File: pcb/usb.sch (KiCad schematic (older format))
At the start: 0 parts

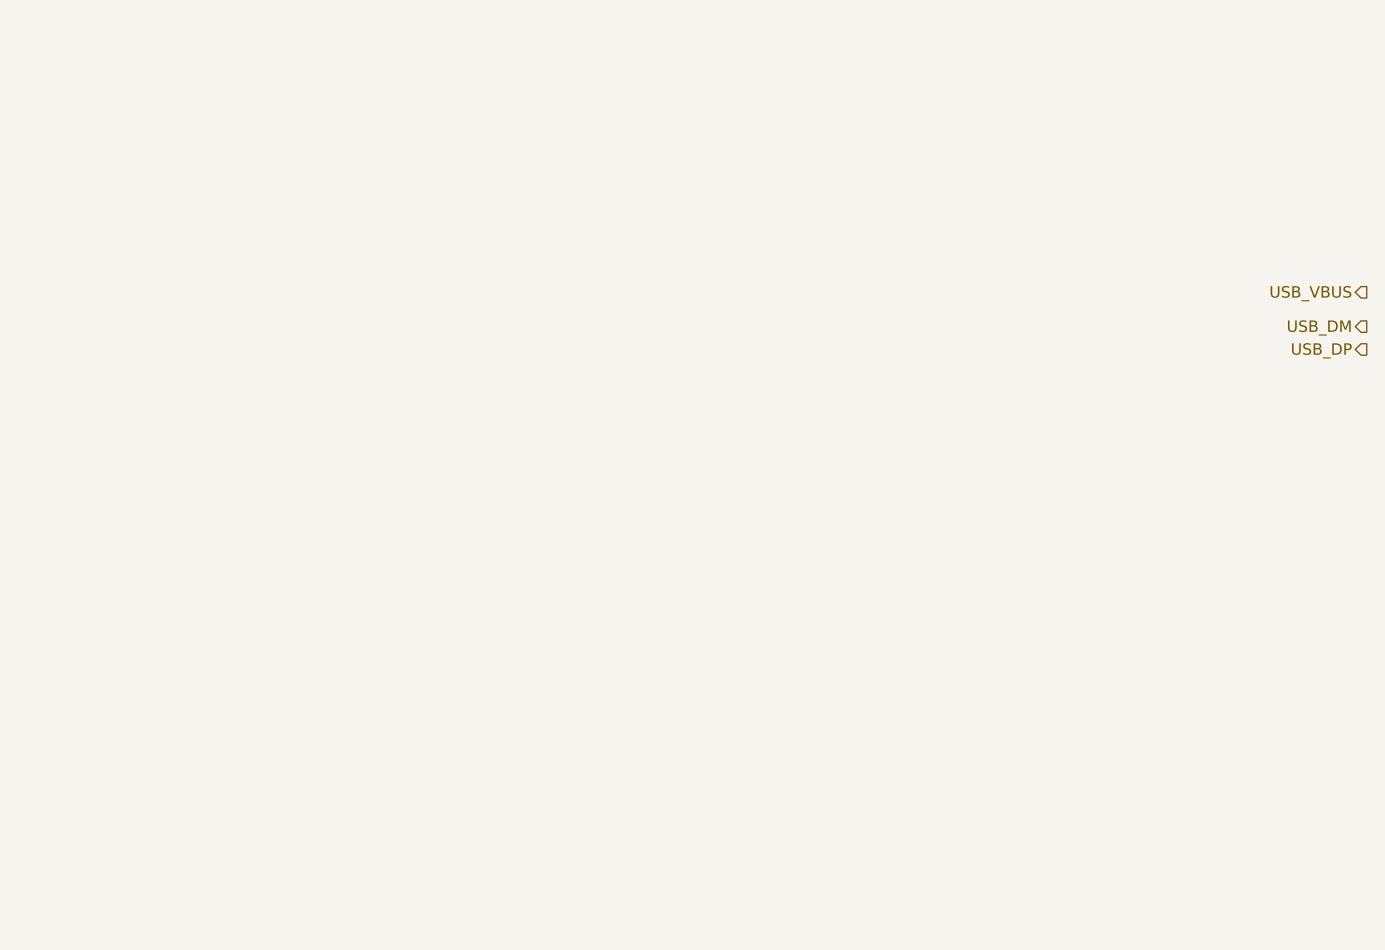
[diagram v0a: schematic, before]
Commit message: SCH: missing signal logic and level shifting
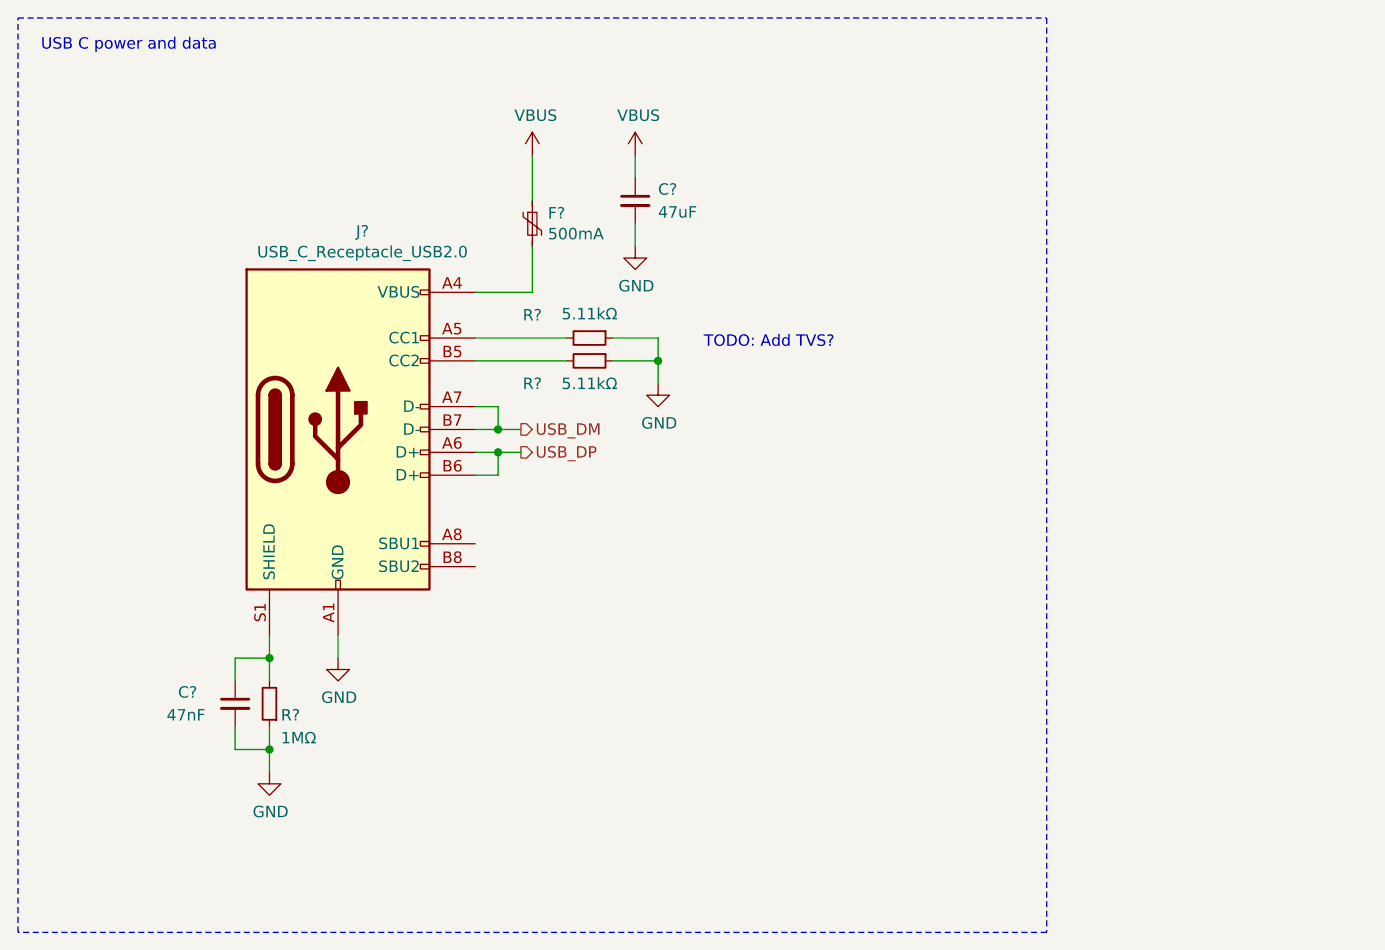
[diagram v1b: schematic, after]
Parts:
- added C?: 47nF, symbol Device:C_Small
- added C?: 47uF, symbol Device:C_Small
- added F?: 500mA, symbol Device:Polyfuse_Small
- added J?: USB_C_Receptacle_USB2.0, symbol Connector:USB_C_Receptacle_USB2.0
- added R? (x2): 5.11kΩ, symbol Device:R_Small
- added R?: 1MΩ, symbol Device:R_Small
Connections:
- net USB_DM: now also J?.A7 (D-), J?.B7 (D-)
- net USB_DP: now also J?.A6 (D+), J?.B6 (D+)
- new net: F?.2, J?.A4 (VBUS), J?.A9 (VBUS), J?.B4 (VBUS), J?.B9 (VBUS)
- new net: J?.A5 (CC1), R?.2
- new net: J?.B5 (CC2), R?.2
- new net: C?.1, J?.S1 (SHIELD), R?.2
- new net GND: C?.2, C?.2, J?.A1 (GND), J?.A12 (GND), J?.B1 (GND), J?.B12 (GND), R?.1, R?.1, R?.1
- new net VBUS: C?.1, F?.1
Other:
- note added: "TODO: Add TVS?\n"
- note added: "USB C power and data"
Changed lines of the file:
@@
 $Descr A4 11693 8268
 encoding utf-8
-Sheet 2 8
-Title ""
-Date ""
-Rev ""
-Comp ""
-Comment1 ""
+Sheet 6 7
+Title "Modular-programmer"
+Date "2020-03-03"
+Rev "1.0"
+Comp "Pepetech"
+Comment1 "Creative Commons Attribution-ShareAlike 4.0 International License"
 Comment2 ""
-Comment3 ""
-Comment4 ""
+Comment3 "Co-designer: João Silva"
+Comment4 "Designer: Rafael Silva"
 $EndDescr
-Text HLabel 9400 2850 0    50   Output ~ 0
+Text HLabel 5700 3300 2    50   Output ~ 0
 USB_DM
-Text HLabel 9400 2950 0    50   Output ~ 0
+Text HLabel 5700 3400 2    50   Output ~ 0
 USB_DP
-Text HLabel 9400 2700 0    50   Output ~ 0
-USB_VBUS
+$Comp
+L Connector:USB_C_Receptacle_USB2.0 J?
+U 1 1 5E6B6DFC
+P 4900 3300
+F 0 "J?" H 5007 4167 50  0000 C CNN
+F 1 "USB_C_Receptacle_USB2.0" H 5007 4076 50  0000 C CNN
+F 2 "" H 5050 3300 50  0001 C CNN
+F 3 "https://www.usb.org/sites/default/files/documents/usb_type-c.zip" H 5050 3300 50  0001 C CNN
+	1    4900 3300
+	1    0    0    -1
+$EndComp
+Wire Wire Line
+	5500 3400 5600 3400
+Wire Wire Line
+	5500 3500 5600 3500
+Wire Wire Line
+	5600 3500 5600 3400
+Connection ~ 5600 3400
+Wire Wire Line
+	5600 3400 5700 3400
+Wire Wire Line
+	5500 3200 5600 3200
+Wire Wire Line
+	5600 3200 5600 3300
+Wire Wire Line
+	5600 3300 5700 3300
+Wire Wire Line
+	5500 3300 5600 3300
+Connection ~ 5600 3300
+Wire Wire Line
+	5750 2700 5750 2500
+$Comp
+L Device:Polyfuse_Small F?
+U 1 1 5E6B9537
+P 5750 2400
+F 0 "F?" H 5818 2446 50  0000 L CNN
+F 1 "500mA" H 5818 2355 50  0000 L CNN
+F 2 "" H 5800 2200 50  0001 L CNN
+F 3 "~" H 5750 2400 50  0001 C CNN
+	1    5750 2400
+	1    0    0    -1
+$EndComp
+Wire Wire Line
+	5750 2300 5750 2100
+$Comp
+L Device:R_Small R?
+U 1 1 5E6BB888
+P 6000 2900
+F 0 "R?" V 5900 2650 50  0000 C CNN
+F 1 "5.11kΩ" V 5895 2900 50  0000 C CNN
+F 2 "" H 6000 2900 50  0001 C CNN
+F 3 "~" H 6000 2900 50  0001 C CNN
+	1    6000 2900
+	0    1    1    0
+$EndComp
+$Comp
+L Device:R_Small R?
+U 1 1 5E6BC592
+P 6000 3000
+F 0 "R?" V 6100 2750 50  0000 C CNN
+F 1 "5.11kΩ" V 6100 3000 50  0000 C CNN
+F 2 "" H 6000 3000 50  0001 C CNN
+F 3 "~" H 6000 3000 50  0001 C CNN
+	1    6000 3000
+	0    1    1    0
+$EndComp
+Wire Wire Line
+	6100 2900 6300 2900
+Wire Wire Line
+	6300 2900 6300 3000
+Wire Wire Line
+	6100 3000 6300 3000
+Connection ~ 6300 3000
+Wire Wire Line
+	6300 3000 6300 3100
+$Comp
+L power:GND #PWR?
+U 1 1 5E6BE57B
+P 6300 3100
+F 0 "#PWR?" H 6300 2850 50  0001 C CNN
+F 1 "GND" H 6305 2927 50  0000 C CNN
+F 2 "" H 6300 3100 50  0001 C CNN
+F 3 "" H 6300 3100 50  0001 C CNN
+	1    6300 3100
+	1    0    0    -1
+$EndComp
+Wire Wire Line
+	4900 4200 4900 4300
+Wire Wire Line
+	4600 4200 4600 4300
+Wire Wire Line
+	4600 4300 4450 4300
+Wire Wire Line
+	4450 4300 4450 4400
+Connection ~ 4600 4300
+Wire Wire Line
+	4600 4300 4600 4400
+$Comp
+L Device:R_Small R?
+U 1 1 5E6BF283
+P 4600 4500
+F 0 "R?" H 4550 4550 50  0000 R CNN
+F 1 "1MΩ" H 4550 4650 50  0000 R CNN
+F 2 "" H 4600 4500 50  0001 C CNN
+F 3 "~" H 4600 4500 50  0001 C CNN
+	1    4600 4500
+	-1   0    0    1
+$EndComp
+$Comp
+L Device:C_Small C?
+U 1 1 5E6BFCD2
+P 4450 4500
+F 0 "C?" H 4200 4550 50  0000 L CNN
+F 1 "47nF" H 4150 4450 50  0000 L CNN
+F 2 "" H 4450 4500 50  0001 C CNN
+F 3 "~" H 4450 4500 50  0001 C CNN
+	1    4450 4500
+	1    0    0    -1
+$EndComp
+Wire Wire Line
+	4450 4600 4450 4700
+Wire Wire Line
+	4450 4700 4600 4700
+Wire Wire Line
+	4600 4700 4600 4800
+Wire Wire Line
+	4600 4600 4600 4700
+Connection ~ 4600 4700
+$Comp
+L power:GND #PWR?
+U 1 1 5E6C0B4E
+P 4600 4800
+F 0 "#PWR?" H 4600 4550 50  0001 C CNN
+F 1 "GND" H 4605 4627 50  0000 C CNN
+F 2 "" H 4600 4800 50  0001 C CNN
+F 3 "" H 4600 4800 50  0001 C CNN
+	1    4600 4800
+	1    0    0    -1
+$EndComp
+$Comp
+L power:GND #PWR?
+U 1 1 5E6C1141
+P 4900 4300
+F 0 "#PWR?" H 4900 4050 50  0001 C CNN
+F 1 "GND" H 4905 4127 50  0000 C CNN
+F 2 "" H 4900 4300 50  0001 C CNN
+F 3 "" H 4900 4300 50  0001 C CNN
+	1    4900 4300
+	1    0    0    -1
+$EndComp
+$Comp
+L power:VBUS #PWR?
+U 1 1 5E8C6541
+P 5750 2100
+F 0 "#PWR?" H 5750 1950 50  0001 C CNN
+F 1 "VBUS" H 5765 2273 50  0000 C CNN
+F 2 "" H 5750 2100 50  0001 C CNN
+F 3 "" H 5750 2100 50  0001 C CNN
+	1    5750 2100
+	1    0    0    -1
+$EndComp
+Wire Notes Line
+	3500 1500 8000 1500
+Wire Notes Line
+	8000 1500 8000 5500
+Wire Notes Line
+	8000 5500 3500 5500
+Wire Notes Line
+	3500 5500 3500 1500
+Text Notes 3600 1650 0    50   ~ 0
+USB C power and data
+$Comp
+L power:VBUS #PWR?
+U 1 1 5E950B45
+P 6200 2100
+F 0 "#PWR?" H 6200 1950 50  0001 C CNN
+F 1 "VBUS" H 6215 2273 50  0000 C CNN
+F 2 "" H 6200 2100 50  0001 C CNN
+F 3 "" H 6200 2100 50  0001 C CNN
+	1    6200 2100
+	1    0    0    -1
+$EndComp
+Wire Wire Line
+	6200 2100 6200 2200
+$Comp
+L Device:C_Small C?
+U 1 1 5E9512A0
+P 6200 2300
+F 0 "C?" H 6300 2350 50  0000 L CNN
+F 1 "47uF" H 6300 2250 50  0000 L CNN
+F 2 "" H 6200 2300 50  0001 C CNN
+F 3 "~" H 6200 2300 50  0001 C CNN
+	1    6200 2300
+	1    0    0    -1
+$EndComp
+Wire Wire Line
+	6200 2400 6200 2500
+$Comp
+L power:GND #PWR?
+U 1 1 5E952003
+P 6200 2500
+F 0 "#PWR?" H 6200 2250 50  0001 C CNN
+F 1 "GND" H 6205 2327 50  0000 C CNN
+F 2 "" H 6200 2500 50  0001 C CNN
+F 3 "" H 6200 2500 50  0001 C CNN
+	1    6200 2500
+	1    0    0    -1
+$EndComp
+Text Notes 6500 2950 0    50   ~ 0
+TODO: Add TVS?\n
+Wire Wire Line
+	5750 2700 5500 2700
+Wire Wire Line
+	5500 2900 5900 2900
+Wire Wire Line
+	5500 3000 5900 3000
 $EndSCHEMATC

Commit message: SCH: minor changes
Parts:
- removed F?: 500mA, symbol Device:Polyfuse_Small
- added TH?: Thermistor_PTC, symbol Device:Thermistor_PTC
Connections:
- net VBUS: now also TH?.1
- net at J?.A4 (VBUS), J?.A9 (VBUS), J?.B4 (VBUS)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: now also TH?.2
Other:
- moved on the sheet: C?
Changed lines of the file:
@@
 	5500 3300 5600 3300
 Connection ~ 5600 3300
-Wire Wire Line
-	5750 2700 5750 2500
-$Comp
-L Device:Polyfuse_Small F?
-U 1 1 5E6B9537
-P 5750 2400
-F 0 "F?" H 5818 2446 50  0000 L CNN
-F 1 "500mA" H 5818 2355 50  0000 L CNN
-F 2 "" H 5800 2200 50  0001 L CNN
-F 3 "~" H 5750 2400 50  0001 C CNN
-	1    5750 2400
-	1    0    0    -1
-$EndComp
-Wire Wire Line
-	5750 2300 5750 2100
 $Comp
 L Device:R_Small R?
@@
 L power:VBUS #PWR?
 U 1 1 5E950B45
-P 6200 2100
-F 0 "#PWR?" H 6200 1950 50  0001 C CNN
-F 1 "VBUS" H 6215 2273 50  0000 C CNN
-F 2 "" H 6200 2100 50  0001 C CNN
-F 3 "" H 6200 2100 50  0001 C CNN
-	1    6200 2100
+P 6700 2200
+F 0 "#PWR?" H 6700 2050 50  0001 C CNN
+F 1 "VBUS" H 6715 2373 50  0000 C CNN
+F 2 "" H 6700 2200 50  0001 C CNN
+F 3 "" H 6700 2200 50  0001 C CNN
+	1    6700 2200
 	1    0    0    -1
 $EndComp
 Wire Wire Line
-	6200 2100 6200 2200
+	6700 2200 6700 2300
 $Comp
 L Device:C_Small C?
 U 1 1 5E9512A0
-P 6200 2300
-F 0 "C?" H 6300 2350 50  0000 L CNN
-F 1 "47uF" H 6300 2250 50  0000 L CNN
-F 2 "" H 6200 2300 50  0001 C CNN
-F 3 "~" H 6200 2300 50  0001 C CNN
-	1    6200 2300
+P 6700 2400
+F 0 "C?" H 6800 2450 50  0000 L CNN
+F 1 "47uF" H 6800 2350 50  0000 L CNN
+F 2 "" H 6700 2400 50  0001 C CNN
+F 3 "~" H 6700 2400 50  0001 C CNN
+	1    6700 2400
 	1    0    0    -1
 $EndComp
 Wire Wire Line
-	6200 2400 6200 2500
+	6700 2500 6700 2600
 $Comp
 L power:GND #PWR?
 U 1 1 5E952003
-P 6200 2500
-F 0 "#PWR?" H 6200 2250 50  0001 C CNN
-F 1 "GND" H 6205 2327 50  0000 C CNN
-F 2 "" H 6200 2500 50  0001 C CNN
-F 3 "" H 6200 2500 50  0001 C CNN
-	1    6200 2500
+P 6700 2600
+F 0 "#PWR?" H 6700 2350 50  0001 C CNN
+F 1 "GND" H 6705 2427 50  0000 C CNN
+F 2 "" H 6700 2600 50  0001 C CNN
+F 3 "" H 6700 2600 50  0001 C CNN
+	1    6700 2600
 	1    0    0    -1
 $EndComp
@@
 Wire Wire Line
 	5500 3000 5900 3000
+$Comp
+L Device:Thermistor_PTC TH?
+U 1 1 5EB8559A
+P 5750 2400
+F 0 "TH?" H 5848 2446 50  0000 L CNN
+F 1 "Thermistor_PTC" H 5848 2355 50  0000 L CNN
+F 2 "" H 5800 2200 50  0001 L CNN
+F 3 "~" H 5750 2400 50  0001 C CNN
+	1    5750 2400
+	1    0    0    -1
+$EndComp
+Wire Wire Line
+	5750 2250 5750 2100
+Wire Wire Line
+	5750 2700 5750 2550
 $EndSCHEMATC

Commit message: SCH: slight changes
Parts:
- removed C?: 47uF, symbol Device:C_Small
- added C602: 10nF, Capacitor_SMD:C_0603_1608Metric_Pad1.05x0.95mm_HandSolder, symbol Device:C_Small
- added D601, D602: PGB1010603, Diode_SMD:D_0603_1608Metric_Pad1.05x0.95mm_HandSolder, symbol Device:D_TVS_ALT
- added FB601: 600R/0.5A, Inductor_SMD:L_0603_1608Metric_Pad1.05x0.95mm_HandSolder, symbol Device:Ferrite_Bead_Small
- C601: renamed from C?; footprint (none) -> Capacitor_SMD:C_0603_1608Metric_Pad1.05x0.95mm_HandSolder
- J601: renamed from J?; footprint (none) -> Connector_USB:USB_C_Receptacle_HRO_TYPE-C-31-M-12
- R601: renamed from R?; footprint (none) -> Resistor_SMD:R_0603_1608Metric_Pad1.05x0.95mm_HandSolder
- R602, R603: renamed from R?; value 5.11kΩ -> 5.1kΩ; footprint (none) -> Resistor_SMD:R_0603_1608Metric_Pad1.05x0.95mm_HandSolder
- TH601: renamed from TH?; value Thermistor_PTC -> 500mA; footprint (none) -> Fuse:Fuse_0805_2012Metric_Pad1.15x1.40mm_HandSolder
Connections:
- net GND: now also C602.2, D601.2 (A2), D602.2 (A2)
- net USB_DM: now also D602.1 (A1)
- net USB_DP: now also D601.1 (A1)
- net at J601.A4 (VBUS), J601.A9 (VBUS), J601.B4 (VBUS)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: now also C602.1, FB601.1; no longer TH601.2
- new net: FB601.2, TH601.2
- no-connect marks 0 -> 2
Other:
- note removed: "TODO: Add TVS?\n"
- moved on the sheet: R602, R603, TH601
